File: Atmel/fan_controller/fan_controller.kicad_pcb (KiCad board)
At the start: 2 copper layers, 35 x 14 mm, 24 parts, among them J1 I2C, J2 FAN, J3 POT, J4 AVR-ISP-6, J5 PWR, J6 I2C_PWR, Q1 Q_PMOS_GSD, Q2 BC817, U1 LM1117-5.0, U2 ATtiny45-20P, U3 ATtiny13V-10S

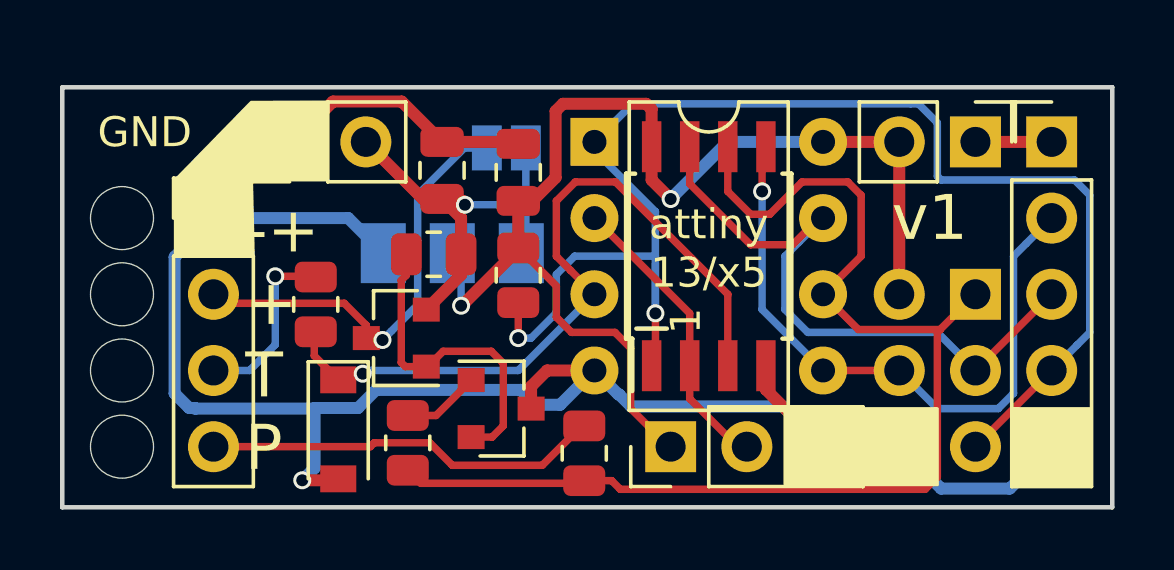
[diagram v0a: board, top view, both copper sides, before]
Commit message: Fixing the SOT23 footprint so that BC817 works properly, adding a TACH pullup, rerouting the board to fit it and moving silkscreen stuff around
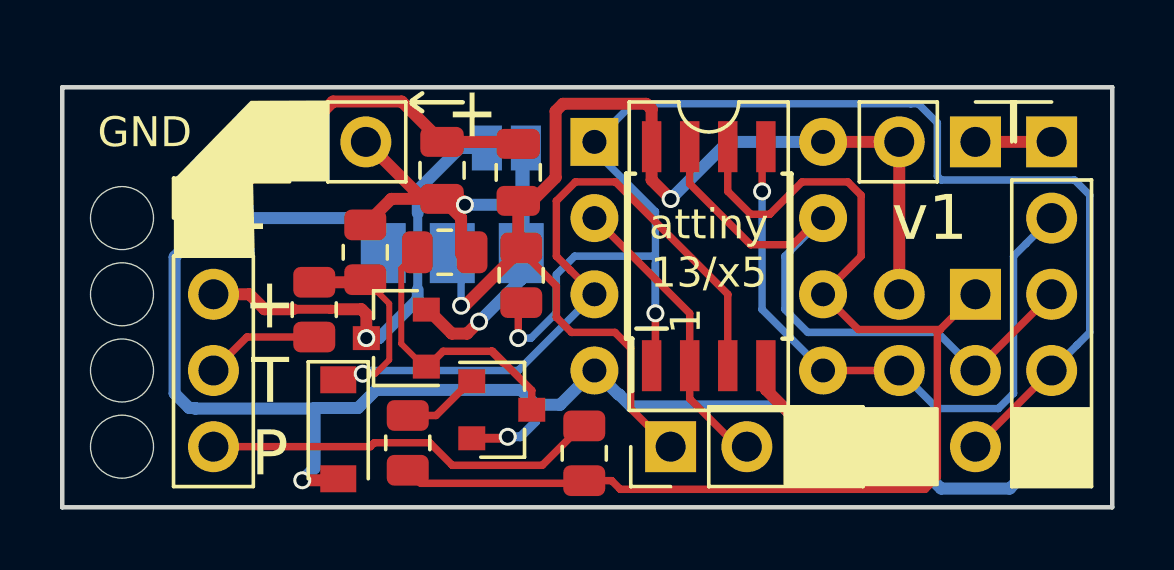
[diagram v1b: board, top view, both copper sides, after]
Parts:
- added R6: 10K, Resistor_SMD:R_0805_2012Metric, F.Cu at (134.6, 87.5)
- moved R1 0.37 mm to (137.2, 87.5)
- moved R4 0.18 mm to (132.9, 89.4), turned to 270 degrees
- moved R3 0.10 mm to (139.8, 88.3)
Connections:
- Q2 pad 2: Net-(Q1-Pad1) -> GND
- Q2 pad 3: GND -> Net-(Q1-Pad1)
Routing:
- net VCC: track 14.3 -> 25.3 mm, vias 1 -> 2
- net TACH: track 25.2 -> 29.1 mm
- net /TACH_IN: track 6.00 -> 3.82 mm, vias 1 -> 0
- net Net-(Q1-Pad1): track 10.8 -> 9.90 mm
- net GND: track 70.4 -> 70.3 mm, vias 1 -> 2
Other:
- board text added: "+"
- board text added: "+ -"
- board text added: "- +"
- board text added: "T P"
- board text removed: "-+ + T P"
